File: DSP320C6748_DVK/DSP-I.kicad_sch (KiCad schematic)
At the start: 1 part, among them U1 TMS320C6748EZWT4

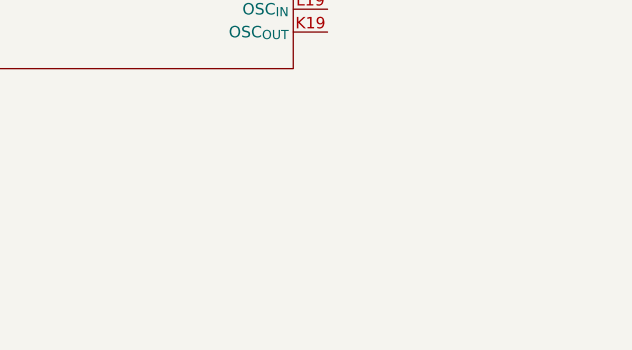
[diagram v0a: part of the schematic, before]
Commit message: TPS650250 Section Added
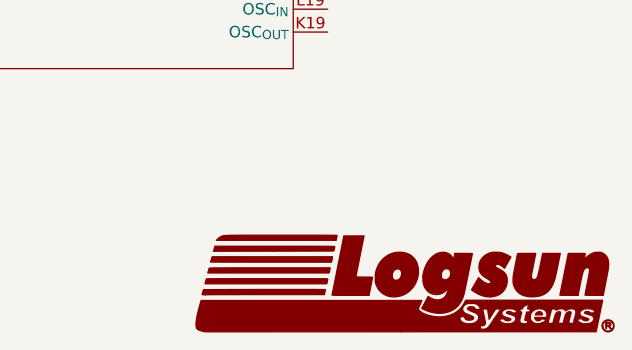
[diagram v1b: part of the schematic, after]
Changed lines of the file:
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@@
+		)
+	)
+	(symbol
+		(lib_id "Logsun_Logo:LOGO")
+		(at 260.35 173.99 0)
+		(unit 1)
+		(exclude_from_sim no)
+		(in_bom yes)
+		(on_board yes)
+		(dnp no)
+		(fields_autoplaced yes)
+		(property "Reference" "#G3"
+			(at 260.35 168.025 0)
+			(effects
+				(font
+					(size 1.27 1.27)
+				)
+				(hide yes)
+			)
+		)
+		(property "Value" "LOGO"
+			(at 260.35 179.955 0)
+			(effects
+				(font
+					(size 1.27 1.27)
+				)
+				(hide yes)
+			)
+		)
+		(property "Footprint" ""
+			(at 260.35 173.99 0)
+			(effects
+				(font
+					(size 1.27 1.27)
+				)
+				(hide yes)
+			)
+		)
+		(property "Datasheet" ""
+			(at 260.35 173.99 0)
+			(effects
+				(font
+					(size 1.27 1.27)
+				)
+				(hide yes)
+			)
+		)
+		(property "Description" ""
+			(at 260.35 173.99 0)
+			(effects
+				(font
+					(size 1.27 1.27)
+				)
+				(hide yes)
+			)
+		)
+		(instances
+			(project "DSP320C6748_DVK"
+				(path "/3a70ffc0-9fe7-4a5b-b3c2-23140355df82/7f99a773-2324-4d25-8796-c695cf33a83f"
+					(reference "#G3")
+					(unit 1)
+				)
+			)
 		)
 	)

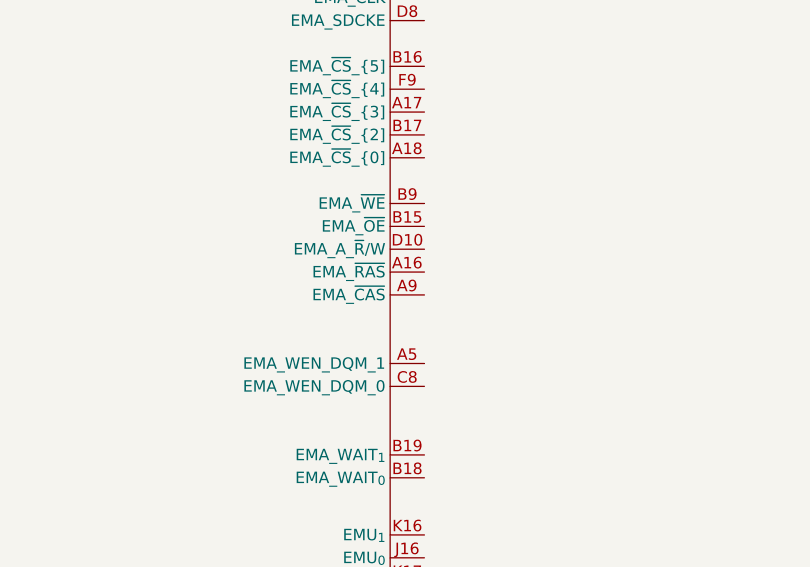
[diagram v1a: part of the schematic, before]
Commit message: POR Generation Section Added
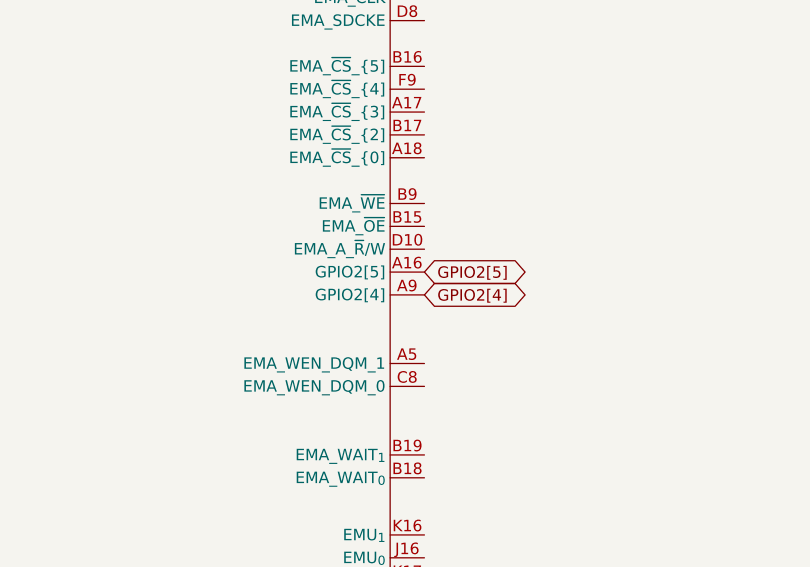
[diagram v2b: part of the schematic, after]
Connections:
- net GPIO2[5]: now reaches U1.A16 (EMA_~{RAS})
- net GPIO2[4]: now reaches U1.A9 (EMA_~{CAS})
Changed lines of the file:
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@@
+		)
+	)
+	(global_label "GPIO2[4]"
+		(shape bidirectional)
+		(at 121.92 82.55 0)
+		(effects
+			(font
+				(size 1.27 1.27)
+			)
+			(justify left)
+		)
+		(property "Intersheetrefs" "${INTERSHEET_REFS}"
+			(at 121.92 82.55 0)
+			(effects
+				(font
+					(size 1.27 1.27)
+				)
+				(hide yes)
+			)
+		)
+	)
+	(global_label "GPIO2[5]"
+		(shape bidirectional)
+		(at 121.92 80.01 0)
+		(effects
+			(font
+				(size 1.27 1.27)
+			)
+			(justify left)
+		)
+		(property "Intersheetrefs" "${INTERSHEET_REFS}"
+			(at 121.92 80.01 0)
+			(effects
+				(font
+					(size 1.27 1.27)
+				)
+				(hide yes)
+			)
 		)
 	)
@@
 		)
 		(pin "A16"
+			(alternate "GPIO2[5]")
 		)
 		(pin "A13"
@@
 		)
 		(pin "A9"
+			(alternate "GPIO2[4]")
 		)
 		(pin "A5"

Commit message: Serial Circuit completed, SATA section Added, DSP Reset Section Added
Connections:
- net ~{BRD_RST}: now reaches U1.K14 (~{RESET})
- net ~{DSP_RST_{OUT}}: now reaches U1.T17 (~{RESETOUT})
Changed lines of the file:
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@@
 (kicad_sch
-	(version 20250114)
+	(version 20260306)
 	(generator "eeschema")
-	(generator_version "9.0")
+	(generator_version "10.0")
 	(paper "A4")
 	(title_block
@@
 		(company "Logsun Systems")
 	)
+	(wire
+		(pts
+			(xy 134.62 119.38) (xy 121.92 119.38)
+		)
+		(stroke
+			(width 0)
+			(type default)
+		)
+	)
 	(global_label "USB_{0}_DP"
 		(shape bidirectional)
@@
 		(property "Intersheetrefs" "${INTERSHEET_REFS}"
 			(at 251.46 113.03 0)
-			(effects
-				(font
-					(size 1.27 1.27)
-				)
-				(hide yes)
+			(hide yes)
+			(show_name no)
+			(do_not_autoplace no)
+			(effects
+				(font
+					(size 1.27 1.27)
+				)
 			)
 		)
@@
 		(property "Intersheetrefs" "${INTERSHEET_REFS}"
 			(at 251.46 110.49 0)
-			(effects
-				(font
-					(size 1.27 1.27)
-				)
-				(hide yes)
+			(hide yes)
+			(show_name no)
+			(do_not_autoplace no)
+			(effects
+				(font
+					(size 1.27 1.27)
+				)
 			)
 		)
@@
 		(property "Intersheetrefs" "${INTERSHEET_REFS}"
 			(at 251.46 105.41 0)
-			(effects
-				(font
-					(size 1.27 1.27)
-				)
-				(hide yes)
+			(hide yes)
+			(show_name no)
+			(do_not_autoplace no)
+			(effects
+				(font
+					(size 1.27 1.27)
+				)
+			)
+		)
+	)
+	(global_label "~{DSP_RST_{OUT}}"
+		(shape input)
+		(at 134.62 119.38 0)
+		(fields_autoplaced yes)
+		(effects
+			(font
+				(size 1.27 1.27)
+				(thickness 0.254)
+				(bold yes)
+			)
+			(justify left)
+		)
+		(property "Intersheetrefs" "${INTERSHEET_REFS}"
+			(at 149.1991 119.38 0)
+			(hide yes)
+			(show_name no)
+			(do_not_autoplace no)
+			(effects
+				(font
+					(size 1.27 1.27)
+				)
+				(justify left)
 			)
 		)
@@
 		(property "Intersheetrefs" "${INTERSHEET_REFS}"
 			(at 251.46 115.57 0)
-			(effects
-				(font
-					(size 1.27 1.27)
-				)
-				(hide yes)
+			(hide yes)
+			(show_name no)
+			(do_not_autoplace no)
+			(effects
+				(font
+					(size 1.27 1.27)
+				)
 			)
 		)
@@
 		(property "Intersheetrefs" "${INTERSHEET_REFS}"
 			(at 121.92 82.55 0)
-			(effects
-				(font
-					(size 1.27 1.27)
-				)
-				(hide yes)
+			(hide yes)
+			(show_name no)
+			(do_not_autoplace no)
+			(effects
+				(font
+					(size 1.27 1.27)
+				)
+			)
+		)
+	)
+	(global_label "~{BRD_RST}"
+		(shape input)
+		(at 121.92 121.92 0)
+		(fields_autoplaced yes)
+		(effects
+			(font
+				(size 1.27 1.27)
+				(thickness 0.254)
+				(bold yes)
+			)
+			(justify left)
+		)
+		(property "Intersheetrefs" "${INTERSHEET_REFS}"
+			(at 133.6059 121.92 0)
+			(hide yes)
+			(show_name no)
+			(do_not_autoplace no)
+			(effects
+				(font
+					(size 1.27 1.27)
+				)
+				(justify left)
 			)
 		)
@@
 		(property "Intersheetrefs" "${INTERSHEET_REFS}"
 			(at 121.92 80.01 0)
-			(effects
-				(font
-					(size 1.27 1.27)
-				)
-				(hide yes)
+			(hide yes)
+			(show_name no)
+			(do_not_autoplace no)
+			(effects
+				(font
+					(size 1.27 1.27)
+				)
 			)
 		)
@@
 		(at 95.25 110.49 0)
 		(unit 2)
+		(body_style 1)
 		(exclude_from_sim no)
 		(in_bom yes)
 		(on_board yes)
+		(in_pos_files yes)
 		(dnp no)
 		(fields_autoplaced yes)
 		(property "Reference" "U1"
 			(at 90.175 34.29 0)
+			(show_name no)
+			(do_not_autoplace no)
 			(effects
 				(font
@@
 		(property "Value" "TMS320C6748EZWT4"
 			(at 90.175 36.83 0)
+			(show_name no)
+			(do_not_autoplace no)
 			(effects
 				(font
@@
 		(property "Footprint" ""
 			(at 90.17 110.49 0)
-			(effects
-				(font
-					(size 1.27 1.27)
-				)
-				(hide yes)
+			(hide yes)
+			(show_name no)
+			(do_not_autoplace no)
+			(effects
+				(font
+					(size 1.27 1.27)
+				)
 			)
 		)
 		(property "Datasheet" ""
 			(at 90.17 110.49 0)
-			(effects
-				(font
-					(size 1.27 1.27)
-				)
-				(hide yes)
+			(hide yes)
+			(show_name no)
+			(do_not_autoplace no)
+			(effects
+				(font
+					(size 1.27 1.27)
+				)
 			)
 		)
 		(property "Description" ""
 			(at 90.17 110.49 0)
-			(effects
-				(font
-					(size 1.27 1.27)
-				)
-				(hide yes)
+			(hide yes)
+			(show_name no)
+			(do_not_autoplace no)
+			(effects
+				(font
+					(size 1.27 1.27)
+				)
 			)
 		)
@@
 		(at 222.25 107.95 0)
 		(unit 3)
+		(body_style 1)
 		(exclude_from_sim no)
 		(in_bom yes)
 		(on_board yes)
+		(in_pos_files yes)
 		(dnp no)
 		(fields_autoplaced yes)
 		(property "Reference" "U1"
 			(at 217.165 33.02 0)
+			(show_name no)
+			(do_not_autoplace no)
 			(effects
 				(font
@@
 		(property "Value" "TMS320C6748EZWT4"
 			(at 217.165 35.56 0)
+			(show_name no)
+			(do_not_autoplace no)
 			(effects
 				(font
@@
 		(property "Footprint" ""
 			(at 217.17 107.95 0)
-			(effects
-				(font
-					(size 1.27 1.27)
-				)
-				(hide yes)
+			(hide yes)
+			(show_name no)
+			(do_not_autoplace no)
+			(effects
+				(font
+					(size 1.27 1.27)
+				)
 			)
 		)
 		(property "Datasheet" ""
 			(at 217.17 107.95 0)
-			(effects
-				(font
-					(size 1.27 1.27)
-				)
-				(hide yes)
+			(hide yes)
+			(show_name no)
+			(do_not_autoplace no)
+			(effects
+				(font
+					(size 1.27 1.27)
+				)
 			)
 		)
 		(property "Description" ""
 			(at 217.17 107.95 0)
-			(effects
-				(font
-					(size 1.27 1.27)
-				)
-				(hide yes)
+			(hide yes)
+			(show_name no)
+			(do_not_autoplace no)
+			(effects
+				(font
+					(size 1.27 1.27)
+				)
 			)
 		)
@@
 		(at 260.35 173.99 0)
 		(unit 1)
+		(body_style 1)
 		(exclude_from_sim no)
 		(in_bom yes)
 		(on_board yes)
+		(in_pos_files yes)
 		(dnp no)
 		(fields_autoplaced yes)
 		(property "Reference" "#G3"
 			(at 260.35 168.025 0)
-			(effects
-				(font
-					(size 1.27 1.27)
-				)
-				(hide yes)
+			(hide yes)
+			(show_name no)
+			(do_not_autoplace no)
+			(effects
+				(font
+					(size 1.27 1.27)
+				)
 			)
 		)
 		(property "Value" "LOGO"
 			(at 260.35 179.955 0)
-			(effects
-				(font
-					(size 1.27 1.27)
-				)
-				(hide yes)
+			(hide yes)
+			(show_name no)
+			(do_not_autoplace no)
+			(effects
+				(font
+					(size 1.27 1.27)
+				)
 			)
 		)
 		(property "Footprint" ""
 			(at 260.35 173.99 0)
-			(effects
-				(font
-					(size 1.27 1.27)
-				)
-				(hide yes)
+			(hide yes)
+			(show_name no)
+			(do_not_autoplace no)
+			(effects
+				(font
+					(size 1.27 1.27)
+				)
 			)
 		)
 		(property "Datasheet" ""
 			(at 260.35 173.99 0)
-			(effects
-				(font
-					(size 1.27 1.27)
-				)
-				(hide yes)
+			(hide yes)
+			(show_name no)
+			(do_not_autoplace no)
+			(effects
+				(font
+					(size 1.27 1.27)
+				)
 			)
 		)
 		(property "Description" ""
 			(at 260.35 173.99 0)
-			(effects
-				(font
-					(size 1.27 1.27)
-				)
-				(hide yes)
-			)
-		)
+			(hide yes)
+			(show_name no)
+			(do_not_autoplace no)
+			(effects
+				(font
+					(size 1.27 1.27)
+				)
+			)
+		)
